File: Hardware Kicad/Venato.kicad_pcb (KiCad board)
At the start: 2 copper layers, 84 x 35.3 mm, 24 parts, among them J1 Conn_01x02_Male, J2 Conn_01x02_Male, J3 Conn_01x02_Male, J4 Conn_01x02_Male, J5 Conn_01x02_Male, J6 Conn_01x02_Male, J7 Conn_01x05_Male, U1 LM317_TO-220, U2 MCP6002-xP, U3 MCP6002-xP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

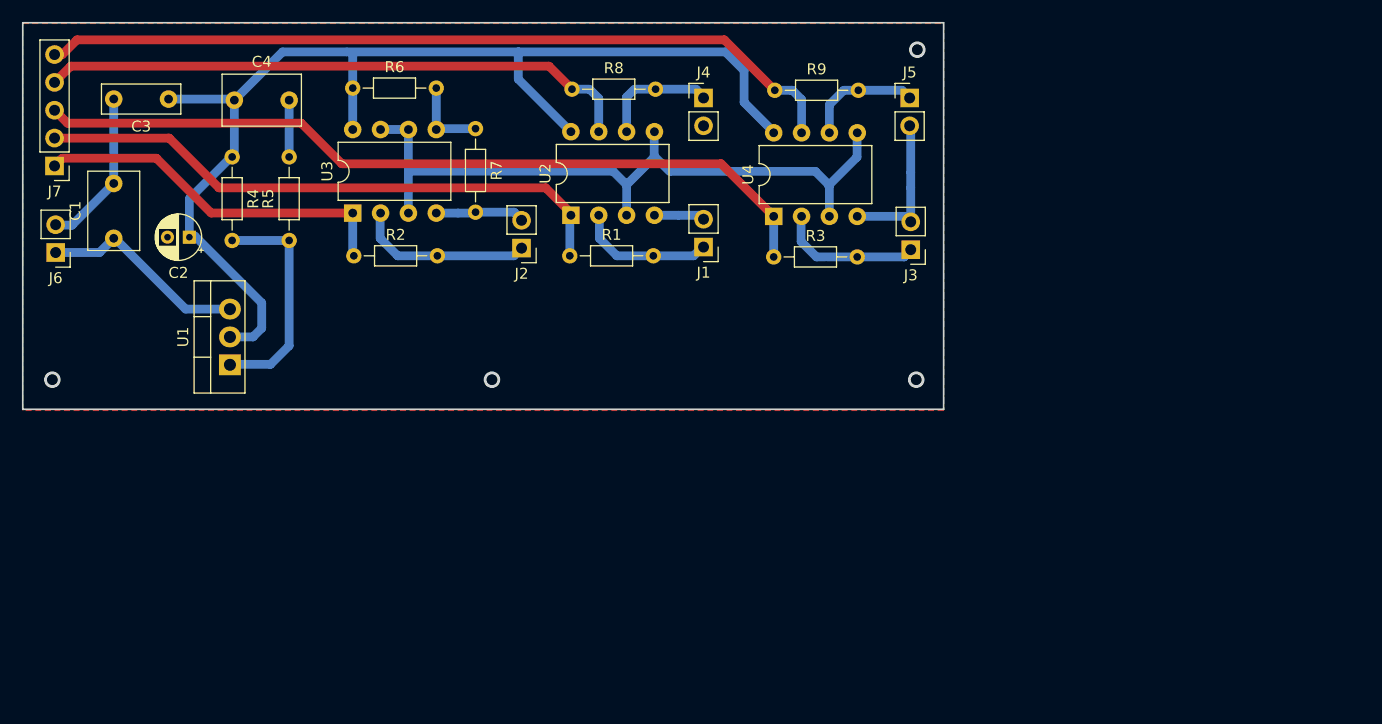
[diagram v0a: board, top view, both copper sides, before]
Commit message: updated arduino code
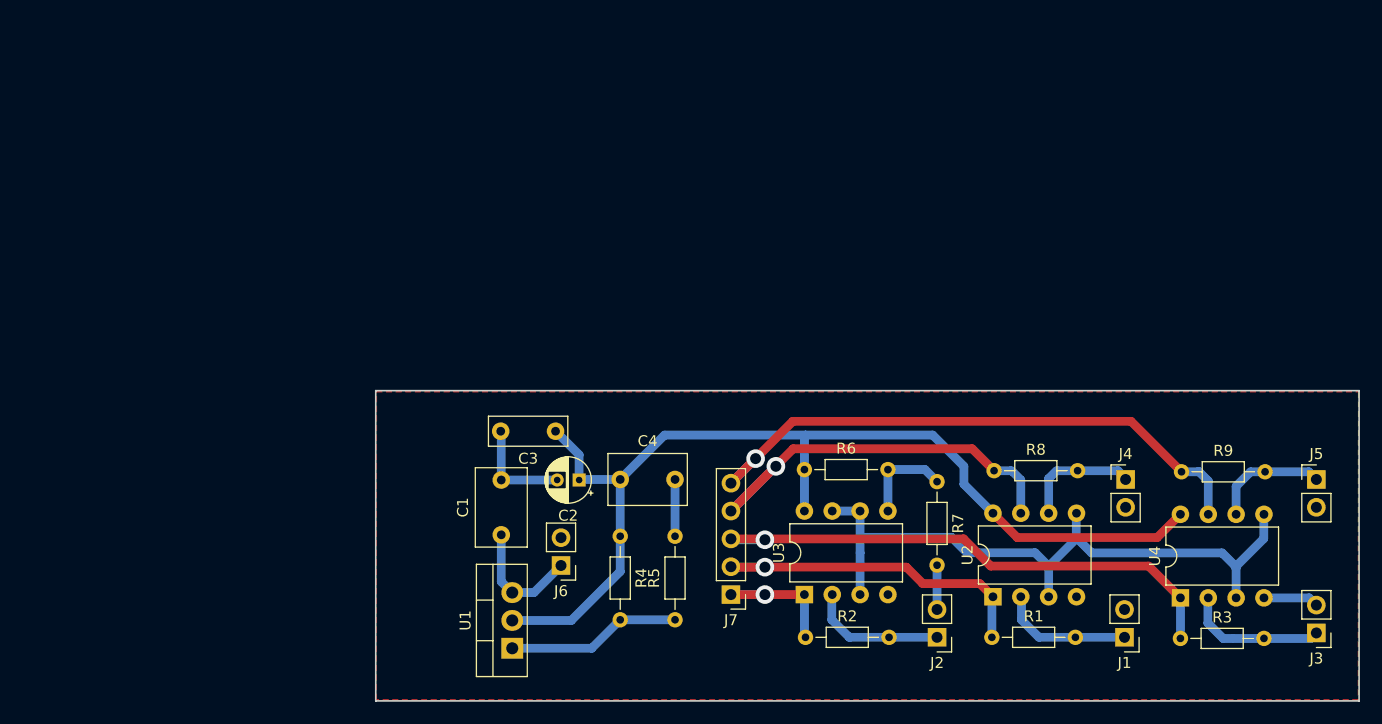
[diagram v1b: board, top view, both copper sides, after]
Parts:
- moved J7 73.0 mm to (77.6, 65.1)
- moved J6 54.2 mm to (62.1, 62.5)
- moved R2 53.9 mm to (84.4, 69.0)
- moved R6 53.9 mm to (84.3, 53.7)
- moved U3 53.9 mm to (84.3, 65.1)
- moved R7 53.0 mm to (96.4, 54.8)
- moved J1 52.4 mm to (113.5, 69.0)
- moved J2 51.9 mm to (96.4, 69.0)
- moved R1 51.9 mm to (101.4, 69.0)
- moved J4 51.9 mm to (113.6, 54.6)
- moved R8 51.9 mm to (101.6, 53.8)
- moved U2 51.9 mm to (101.5, 65.3)
- moved J3 50.9 mm to (131.0, 68.6)
- moved R9 50.9 mm to (118.7, 53.9)
- moved U4 50.9 mm to (118.6, 65.4)
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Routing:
- net SENSE4: track 73.2 -> 50.1 mm, vias 0 -> 1
- net GND: track 46.9 -> 23.9 mm
- net SENSE1: track 53.4 -> 31.9 mm, vias 0 -> 1
- net SENSE2: track 33.5 -> 13.7 mm, vias 0 -> 1
- net SENSE3: track 74.0 -> 54.4 mm, vias 0 -> 1
- net SENSE5: track 54.4 -> 38.7 mm, vias 0 -> 1
- net +3.3VA: track 106.7 -> 94.8 mm
- net +5V: track 19.2 -> 11.2 mm
- net Net-(R4-Pad2): track 20.9 -> 15.9 mm
- net Net-(J2-Pad1): track 16.3 -> 12.6 mm
- net VGND: track 65.0 -> 61.6 mm
- net Net-(R6-Pad2): track 7.42 -> 8.86 mm
- net Net-(J3-Pad1): track 13.1 -> 13.8 mm
- net Net-(J1-Pad1): track 12.8 -> 12.3 mm
- net (no net): vias 4 -> 0
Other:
- board size 84 x 35.3 mm -> 89.7 x 28.3 mm
- board text added: "V"
